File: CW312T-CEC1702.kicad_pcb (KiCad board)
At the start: 4 copper layers, 58.7 x 53.7 mm, 38 parts, among them J1 2Pin_Header_2.54, P1 PCIEx4 EDGE CONNECTOR, U1 CEC1702, U2 SST26VF016B-104I/SN, U3 TXB0104PWR, Y1 32.768kHz

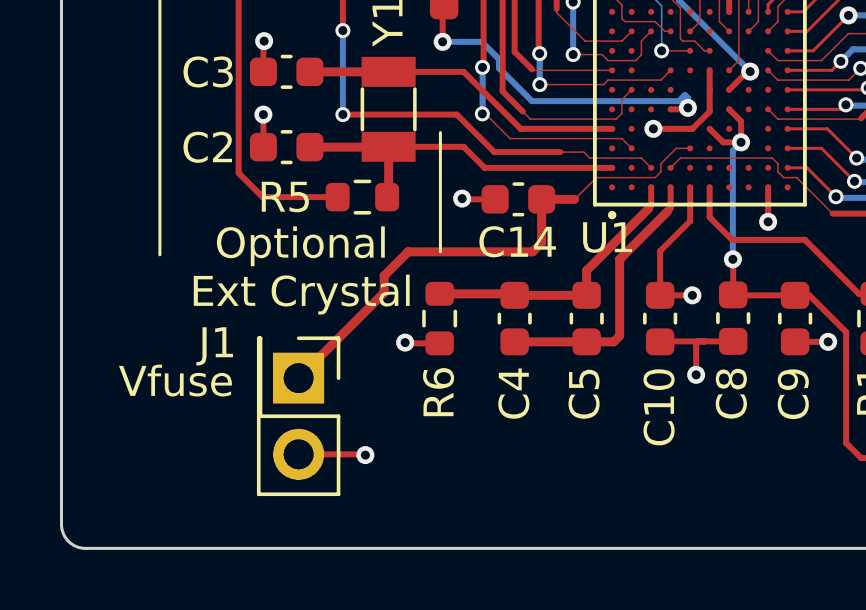
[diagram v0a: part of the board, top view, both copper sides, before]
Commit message: updated schematic and pcb after library re-organization
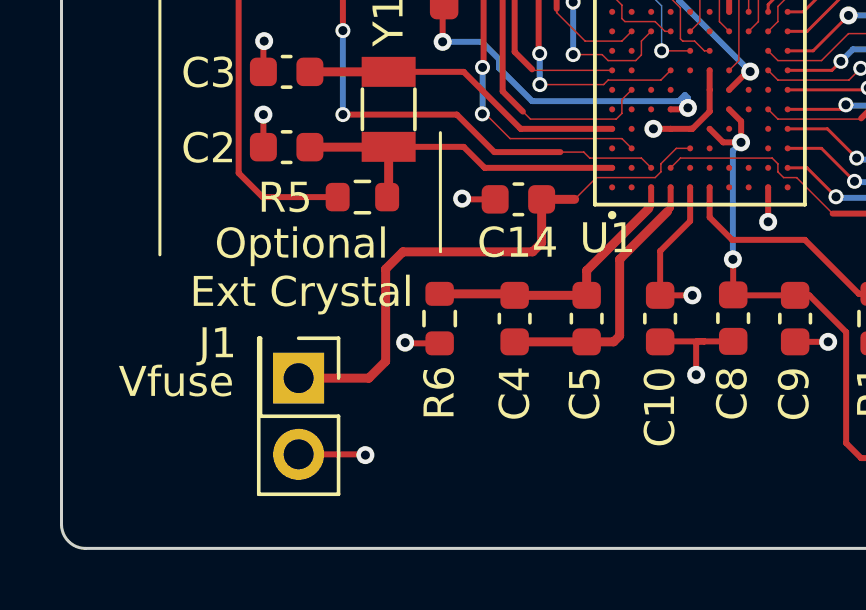
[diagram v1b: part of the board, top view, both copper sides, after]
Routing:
- net Net-(U1-VREF_ADC): track 17.6 -> 19.0 mm
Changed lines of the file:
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@@
 		(tags "capacitor")
 		(property "Reference" "C17"
-			(at 0 -1.43 360)
+			(at 0 -1.43 0)
 			(layer "F.SilkS")
 			(effects
@@
 		)
 		(property "Value" "CAP_2u2_6.3V_0603"
-			(at 0 1.43 360)
+			(at 0 1.43 0)
 			(layer "F.Fab")
 			(effects
@@
 		)
 		(fp_text user "${REFERENCE}"
-			(at 0 0 360)
+			(at 0 0 0)
 			(layer "F.Fab")
 			(effects
@@
 		(tags "capacitor")
 		(property "Reference" "C15"
-			(at 0 -1.500003 360)
+			(at 0 -1.500003 0)
 			(layer "F.SilkS")
 			(effects
@@
 		)
 		(property "Value" "CAP_2u2_6.3V_0603"
-			(at 0 1.43 360)
+			(at 0 1.43 0)
 			(layer "F.Fab")
 			(effects
@@
 		)
 		(fp_text user "${REFERENCE}"
-			(at 0 0 360)
+			(at 0 0 0)
 			(layer "F.Fab")
 			(effects
@@
 		(tags "capacitor")
 		(property "Reference" "C2"
-			(at 2.6 -0.04 360)
+			(at 2.6 -0.04 0)
 			(layer "F.SilkS")
 			(effects
@@
 		)
 		(property "Value" "CAP_10p_50V_0603"
-			(at 0 1.43 360)
+			(at 0 1.43 0)
 			(layer "F.Fab")
 			(effects
@@
 		)
 		(fp_text user "${REFERENCE}"
-			(at 0 0 360)
+			(at 0 0 0)
 			(layer "F.Fab")
 			(effects
@@
 		(tags "resistor")
 		(property "Reference" "R3"
-			(at 2.475 0.05 360)
+			(at 2.475 0.05 0)
 			(layer "F.SilkS")
 			(effects
@@
 		)
 		(property "Value" "RES_100k_0603"
-			(at 0 1.43 360)
+			(at 0 1.43 0)
 			(layer "F.Fab")
 			(effects
@@
 		)
 		(fp_text user "${REFERENCE}"
-			(at 0 0 360)
+			(at 0 0 0)
 			(layer "F.Fab")
 			(effects
@@
 		(tags "resistor")
 		(property "Reference" "R5"
-			(at 2.575 -0.025 360)
+			(at 2.575 -0.025 0)
 			(layer "F.SilkS")
 			(effects
@@
 		)
 		(property "Value" "RES_100R_0603"
-			(at 0 1.43 360)
+			(at 0 1.43 0)
 			(layer "F.Fab")
 			(effects
@@
 		)
 		(fp_text user "${REFERENCE}"
-			(at 0 0 360)
+			(at 0 0 0)
 			(layer "F.Fab")
 			(effects
@@
 		(tags "resistor")
 		(property "Reference" "R8"
-			(at 2.450001 0 360)
+			(at 2.450001 0 0)
 			(layer "F.SilkS")
 			(effects
@@
 		)
 		(property "Value" "RES_910k_0603"
-			(at 0 1.43 360)
+			(at 0 1.43 0)
 			(layer "F.Fab")
 			(effects
@@
 		)
 		(fp_text user "${REFERENCE}"
-			(at 0 0 360)
+			(at 0 0 0)
 			(layer "F.Fab")
 			(effects
@@
 		(tags "resistor")
 		(property "Reference" "R9"
-			(at 0 -1.43 360)
+			(at 0 -1.43 0)
 			(layer "F.SilkS")
 			(effects
@@
 		)
 		(property "Value" "RES_10k_0603"
-			(at 0 1.43 360)
+			(at 0 1.43 0)
 			(layer "F.Fab")
 			(effects
@@
 		)
 		(fp_text user "${REFERENCE}"
-			(at 0 0 360)
+			(at 0 0 0)
 			(layer "F.Fab")
 			(effects
@@
 		(tags "capacitor")
 		(property "Reference" "C3"
-			(at 2.6 -0.04 360)
+			(at 2.6 -0.04 0)
 			(layer "F.SilkS")
 			(effects
@@
 		)
 		(property "Value" "CAP_10p_50V_0603"
-			(at 0 1.43 360)
+			(at 0 1.43 0)
 			(layer "F.Fab")
 			(effects
@@
 		)
 		(fp_text user "${REFERENCE}"
-			(at 0 0 360)
+			(at 0 0 0)
 			(layer "F.Fab")
 			(effects
@@
 		(tags "capacitor")
 		(property "Reference" "C16"
-			(at 0 -1.43 360)
+			(at 0 -1.43 0)
 			(layer "F.SilkS")
 			(effects
@@
 		)
 		(property "Value" "CAP_2u2_6.3V_0603"
-			(at 0 1.43 360)
+			(at 0 1.43 0)
 			(layer "F.Fab")
 			(effects
@@
 		)
 		(fp_text user "${REFERENCE}"
-			(at 0 0 360)
+			(at 0 0 0)
 			(layer "F.Fab")
 			(effects
@@
 		)
 		(fp_text user "${REFERENCE}"
-			(at 1.270001 0 360)
+			(at 1.270001 0 0)
 			(layer "F.Fab")
 			(effects
@@
 		(tags "resistor")
 		(property "Reference" "R10"
-			(at 0 -1.43 360)
+			(at 0 -1.43 0)
 			(layer "F.SilkS")
 			(effects
@@
 		)
 		(property "Value" "RES_100k_0603"
-			(at 0 1.43 360)
+			(at 0 1.43 0)
 			(layer "F.Fab")
 			(effects
@@
 		)
 		(fp_text user "${REFERENCE}"
-			(at 0 0 360)
+			(at 0 0 0)
 			(layer "F.Fab")
 			(effects
@@
 		(tags "capacitor")
 		(property "Reference" "C14"
-			(at -0.025004 1.449999 360)
+			(at -0.025004 1.449999 0)
 			(layer "F.SilkS")
 			(effects
@@
 		)
 		(property "Value" "CAP_100n_50V_0603"
-			(at 0 1.43 360)
+			(at 0 1.43 0)
 			(layer "F.Fab")
 			(effects
@@
 		)
 		(fp_text user "${REFERENCE}"
-			(at 0 0 360)
+			(at 0 0 0)
 			(layer "F.Fab")
 			(effects
@@
 		(tags "net tie solder jumper bridged")
 		(property "Reference" "JP1"
-			(at 0.025001 1.925 360)
+			(at 0.025001 1.925 0)
 			(layer "F.SilkS")
 			(effects
@@
 		)
 		(property "Value" "~"
-			(at 0 1.9 360)
+			(at 0 1.9 0)
 			(layer "F.Fab")
 			(effects
@@
 		(at 130.125 110.075 90)
 		(property "Reference" "U1"
-			(at -4.625 -3.075 360)
+			(at -4.625 -3.075 0)
 			(layer "F.SilkS")
 			(effects
@@
 	)
 	(segment
-		(start 119.6 115.95)
-		(end 119.6 116.51)
+		(start 124.850004 114.849996)
+		(end 124.55 115.15)
 		(width 0.3)
 		(layer "F.Cu")
@@
 	)
 	(segment
-		(start 124.850004 113.400001)
-		(end 124.850004 114.849996)
+		(start 120.225 115.15)
+		(end 119.65 115.725)
+		(width 0.3)
+		(layer "F.Cu")
+		(net 8)
+	)
+	(segment
+		(start 119.65 115.725)
+		(end 119.65 118.8)
 		(width 0.3)
 		(layer "F.Cu")
@@
 	(segment
 		(start 124.55 115.15)
-		(end 120.4 115.15)
+		(end 120.225 115.15)
+		(width 0.3)
+		(layer "F.Cu")
+		(net 8)
+	)
+	(segment
+		(start 119.09 119.36)
+		(end 116.75 119.36)
 		(width 0.3)
 		(layer "F.Cu")
@@
 	)
 	(segment
-		(start 120.4 115.15)
-		(end 119.6 115.95)
-		(width 0.3)
-		(layer "F.Cu")
-		(net 8)
-	)
-	(segment
 		(start 129.8 111.7)
 		(end 129.340379 111.7)
@@
 	)
 	(segment
-		(start 128.825 112.484619)
-		(end 128.634619 112.675)
-		(width 0.05)
+		(start 119.65 118.8)
+		(end 119.09 119.36)
+		(width 0.3)
 		(layer "F.Cu")
 		(net 8)
 	)
 	(segment
-		(start 119.6 116.51)
-		(end 116.75 119.36)
+		(start 124.850004 113.400001)
+		(end 124.850004 114.849996)
 		(width 0.3)
 		(layer "F.Cu")
@@
 	)
 	(segment
-		(start 124.850004 114.849996)
-		(end 124.55 115.15)
-		(width 0.3)
+		(start 128.825 112.484619)
+		(end 128.634619 112.675)
+		(width 0.05)
 		(layer "F.Cu")
 		(net 8)
@@
 		(polygon
 			(pts
-				(xy 106.75 69.925) (xy 169.425 69.925) (xy 169.425 126.975) (xy 169.425 126.975) (xy 106.75 126.975)
-				(xy 106.75 126.975) (xy 106.75 69.925) (xy 106.75 69.925)
+				(xy 106.75 69.925) (xy 169.425 69.925) (xy 169.425 126.975) (xy 106.75 126.975)
 			)
 		)
@@
 		(polygon
 			(pts
-				(xy 105.375 69.1) (xy 170.5 69.1) (xy 170.5 69.1) (xy 170.5 128.4) (xy 170.5 128.4) (xy 105.375 128.4)
-				(xy 105.375 69.1)
+				(xy 105.375 69.1) (xy 170.5 69.1) (xy 170.5 128.4) (xy 105.375 128.4)
 			)
 		)
